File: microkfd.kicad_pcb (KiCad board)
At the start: 2 copper layers, 55 x 25.5 mm, 41 parts, among them J1 USB_B_Micro, J2 AudioJack3, J3 OLED, Q1 2N7002, Q2 2N7002, SW1 RST, SW2 DOWN, SW3 ENT, SW4 UP, U1 SP3003-02, U2 ATmega32U4-AU, Y1 16MHz

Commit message: rev A design done
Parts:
- added G***: LOGO, w3axl-logos:logo-4.2x4.2, B.Cu at (138.0, 94.5)
- added TP1: MOSI, TestPoint:TestPoint_Pad_1.0x1.0mm, B.Cu at (113.2, 110.0)
- added TP2: SCK, TestPoint:TestPoint_Pad_1.0x1.0mm, B.Cu at (115.2, 110.0)
- added TP3: MISO, TestPoint:TestPoint_Pad_1.0x1.0mm, B.Cu at (111.2, 110.0)
- added TP4: RST, TestPoint:TestPoint_Pad_1.0x1.0mm, B.Cu at (117.2, 110.0)
- added TP5: VCC, TestPoint:TestPoint_Pad_1.0x1.0mm, B.Cu at (109.2, 110.0)
- added TP6: GND, TestPoint:TestPoint_Pad_1.0x1.0mm, B.Cu at (119.2, 110.0)
- J1: footprint Connector_USB:USB_Mini-B_Wuerth_65100516121_Horizontal -> Connector_USB:USB_Micro-B_Wuerth_629105150521_CircularHoles
- moved D5 108.9 mm to (140.0, 109.8), turned to 90 degrees
- moved D4 103.8 mm to (134.0, 109.7), turned to 90 degrees
- moved R17 103.4 mm to (137.0, 109.8), turned to 270 degrees
- moved R16 98.9 mm to (131.0, 109.8), turned to 270 degrees
- moved R4 98.4 mm to (124.0, 110.8)
- moved R6 90.0 mm to (124.0, 108.5)
- moved C3 89.8 mm to (107.0, 104.5), turned to 270 degrees
- moved C6 75.0 mm to (99.0, 91.8)
- moved F1 4.74 mm to (94.5, 90.5), turned to 270 degrees
- moved C5 4.50 mm to (127.5, 109.8)
- moved U1 0.75 mm to (99.0, 109.8), turned to 180 degrees
- moved D2 0.56 mm to (137.8, 105.5)
- moved D3 0.56 mm to (93.2, 109.8)
- moved R14 0.56 mm to (133.2, 105.5)
- moved C1 0.35 mm to (119.2, 110.0)
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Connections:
- net Net-(R3-Pad1) renamed RST
- U2 pad 10: LED_PWR -> MOSI
- U2 pad 11: Net-(U2-Pad11) -> MISO
- U2 pad 12: Net-(U2-Pad12) -> LED_PWR
- U2 pad 9: Net-(U2-Pad9) -> SCK
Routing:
- net LED_ACT: track 0.00 -> 36.0 mm, vias 0 -> 2
- net I2C_SCL: track 0.00 -> 34.0 mm, vias 0 -> 2
- net I2C_SDA: track 0.00 -> 29.5 mm, vias 0 -> 2
- net RST: track 0.00 -> 27.9 mm, vias 0 -> 1
- net +5V: track 128.2 -> 148.9 mm, vias 6 -> 7
- net LED_PWR: track 0.00 -> 16.8 mm, vias 0 -> 2
- net Net-(J1-Pad2): track 11.4 -> 27.5 mm
- net LED_SNS: track 0.00 -> 15.1 mm, vias 0 -> 2
- net Net-(J1-Pad3): track 10.5 -> 22.9 mm
- net SCK: track 0.00 -> 11.1 mm, vias 0 -> 1
- net MOSI: track 0.00 -> 9.26 mm, vias 0 -> 1
- net MISO: track 0.00 -> 6.94 mm, vias 0 -> 1
- net Net-(C3-Pad1): track 0.00 -> 5.12 mm
- net Net-(D4-Pad2): track 0.00 -> 3.85 mm
- net Net-(D5-Pad2): track 0.00 -> 3.84 mm
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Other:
- board text added: "5V"
- board text added: "GND"
- board text added: "MISO"
- board text added: "MOSI"
- board text added: "MicroKFD"
- board text added: "RST"
- board text added: "SCK"
- board text added: "rev A 2021-12-06"

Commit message: cleanups and updates
- switched to Kicad 6.0
- removed Kicad 5.x files
- switched to 32u4RC due to availability
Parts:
- U2: value ATmega32U4-AU -> ATmega32U4RC-A
- moved G*** 0.25 mm to (137.8, 94.5), turned to 180 degrees
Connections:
- J1 pad 4: Net-(J1-Pad4) -> unconnected-(J1-Pad4)
- U1 pad 3: Net-(U1-Pad3) -> unconnected-(U1-Pad3)
- U2 pad 20: Net-(U2-Pad20) -> unconnected-(U2-Pad20)
- U2 pad 21: Net-(U2-Pad21) -> unconnected-(U2-Pad21)
- U2 pad 22: Net-(U2-Pad22) -> unconnected-(U2-Pad22)
- U2 pad 26: Net-(U2-Pad26) -> unconnected-(U2-Pad26)
- U2 pad 28: Net-(U2-Pad28) -> unconnected-(U2-Pad28)
- U2 pad 29: Net-(U2-Pad29) -> unconnected-(U2-Pad29)
- U2 pad 30: Net-(U2-Pad30) -> unconnected-(U2-Pad30)
- U2 pad 32: Net-(U2-Pad32) -> unconnected-(U2-Pad32)
- U2 pad 33: Net-(U2-Pad33) -> unconnected-(U2-Pad33)
- U2 pad 39: Net-(U2-Pad39) -> unconnected-(U2-Pad39)
- U2 pad 40: Net-(U2-Pad40) -> unconnected-(U2-Pad40)
- U2 pad 41: Net-(U2-Pad41) -> unconnected-(U2-Pad41)
- U2 pad 8: Net-(U2-Pad8) -> unconnected-(U2-Pad8)
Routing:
- net unconnected-(J1-Pad4): track 0.00 -> 1.92 mm
- net Net-(J1-Pad4): track 1.92 -> 0.00 mm
- net XT2: track 10.8 -> 10.1 mm
- net Net-(U1-Pad3): track 0.65 -> 0.00 mm
- net unconnected-(U1-Pad3): track 0.00 -> 0.60 mm
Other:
- net class Default removed
- board text added: "rev B 2022-01-08"
- board text removed: "rev A 2021-12-06"

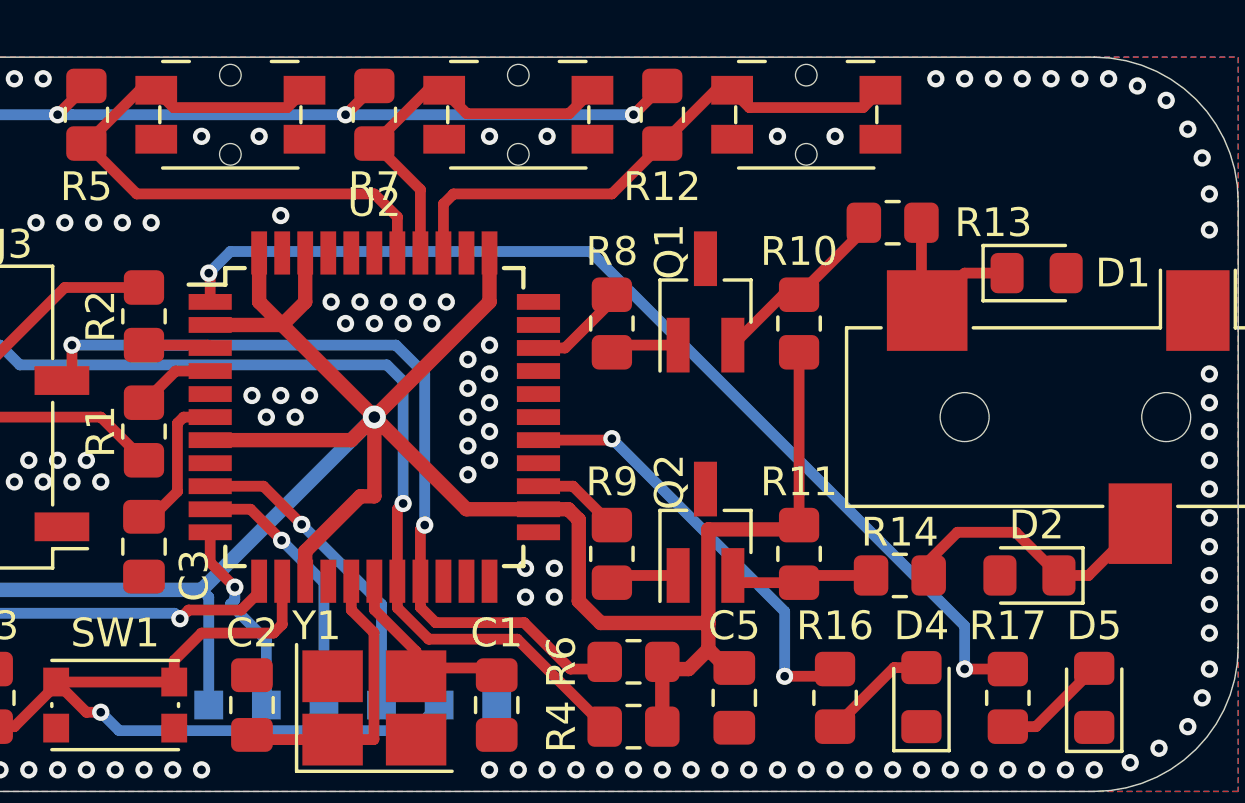
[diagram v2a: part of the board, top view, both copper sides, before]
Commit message: finalized rev B
switched MOSFETs due to parts availability, regenerated gerbers
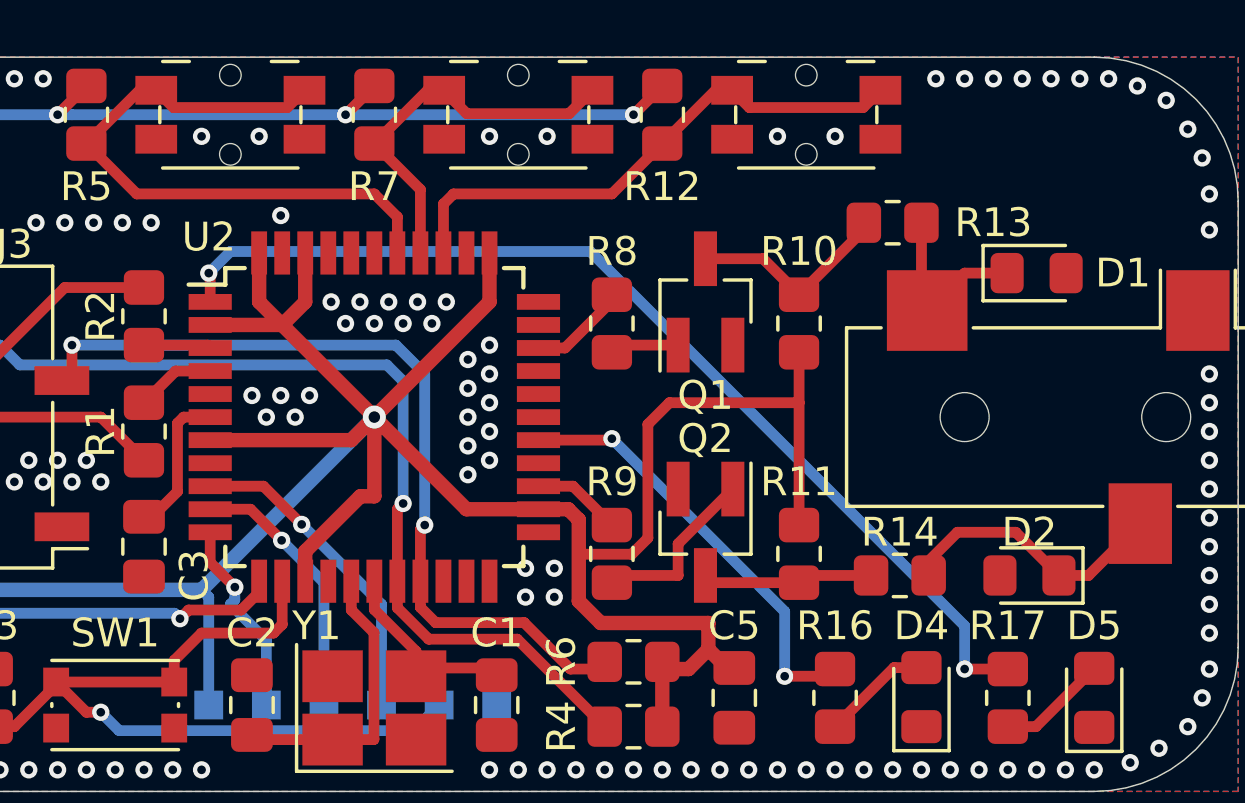
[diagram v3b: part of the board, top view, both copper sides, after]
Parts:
- Q1, Q2: value 2N7002 -> T2N7002
- moved G*** 0.25 mm to (138.0, 94.5)
- turned Q2 to -90 degrees
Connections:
- Q1 pad 2: Net-(Q1-Pad2) -> GND
- Q1 pad 3: GND -> Net-(R10-Pad1)
- Q2 pad 2: Net-(Q2-Pad2) -> GND
- Q2 pad 3: GND -> Net-(R11-Pad1)
- R10 pad 1: Net-(Q1-Pad2) -> Net-(R10-Pad1)
- R11 pad 1: Net-(Q2-Pad2) -> Net-(R11-Pad1)
- R13 pad 1: Net-(Q1-Pad2) -> Net-(R10-Pad1)
- R14 pad 1: Net-(Q2-Pad2) -> Net-(R11-Pad1)
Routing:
- net Net-(R10-Pad1): track 0.00 -> 7.20 mm
- net Net-(Q1-Pad2): track 6.46 -> 0.00 mm
- net Net-(R11-Pad1): track 0.00 -> 5.96 mm
- net +5V: track 148.5 -> 154.1 mm
- net Net-(Q2-Pad2): track 5.01 -> 0.00 mm
- net Net-(R9-Pad1): track 2.40 -> 6.19 mm

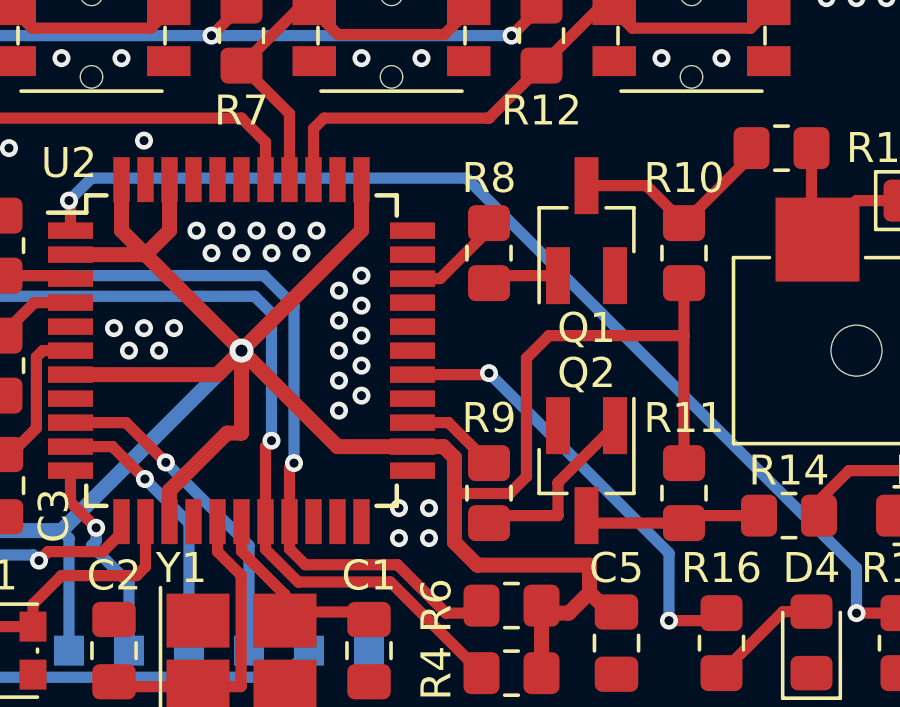
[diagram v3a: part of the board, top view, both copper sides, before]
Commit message: revC updates
fixed missing data input line (now runs to PC2 interrupt pin)
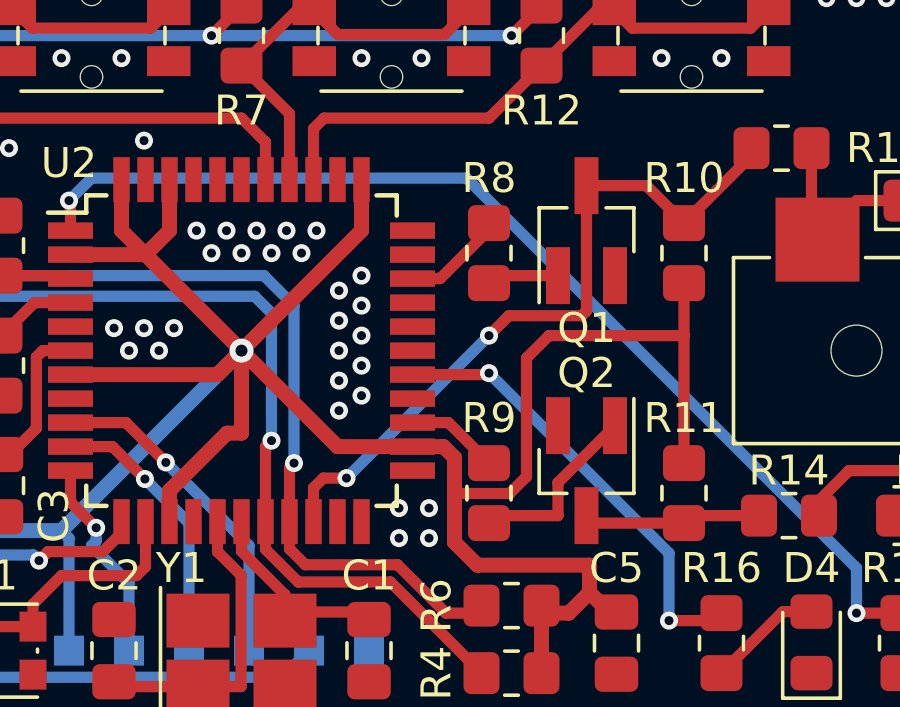
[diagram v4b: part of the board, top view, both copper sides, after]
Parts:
- moved G*** 0.35 mm to (137.8, 94.2)
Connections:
- net DATA renamed DATA_OUT
- Q1 pad 3: Net-(R10-Pad1) -> DATA_IN
- R10 pad 1: Net-(R10-Pad1) -> DATA_IN
- R13 pad 1: Net-(R10-Pad1) -> DATA_IN
- U2 pad 20: unconnected-(U2-Pad20) -> DATA_IN
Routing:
- net DATA_IN: track 0.00 -> 24.0 mm, vias 0 -> 2
- net Net-(R10-Pad1): track 7.20 -> 0.00 mm
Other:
- board text added: "rev C 2022-01-19"
- board text removed: "rev B 2022-01-08"

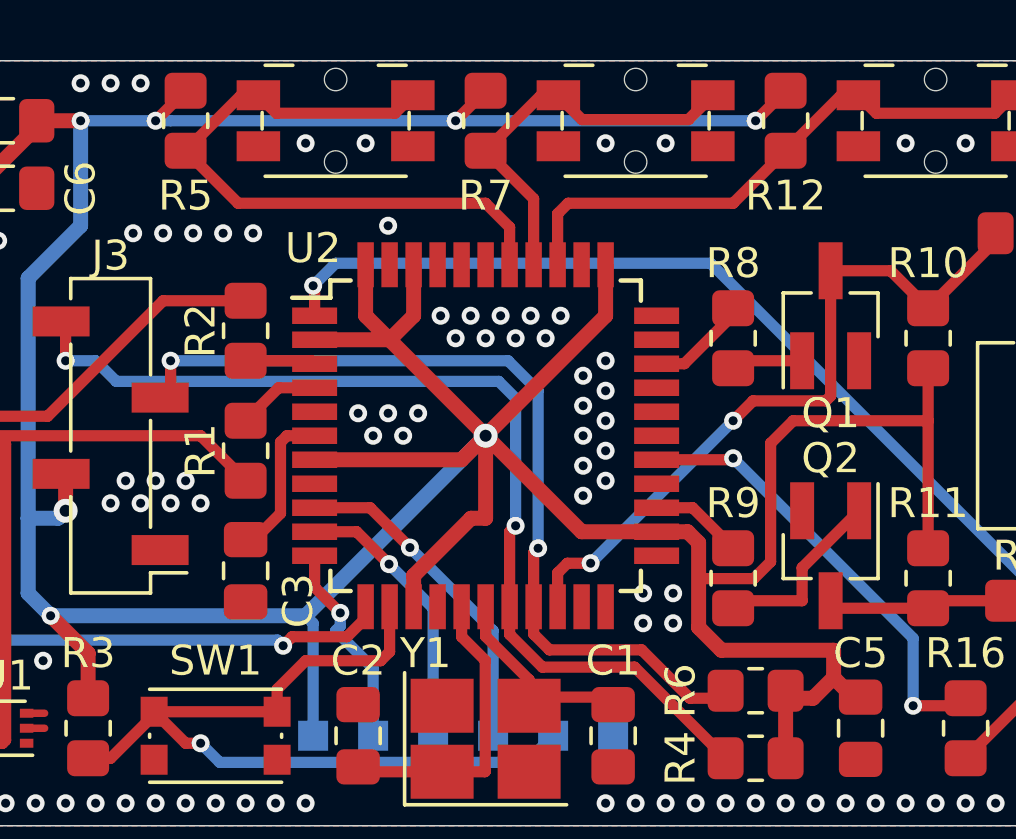
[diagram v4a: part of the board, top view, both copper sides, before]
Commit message: rev D: fixed pin mappings
changed pin mappings to be closer to original KFDShield, added correct sense and data lines
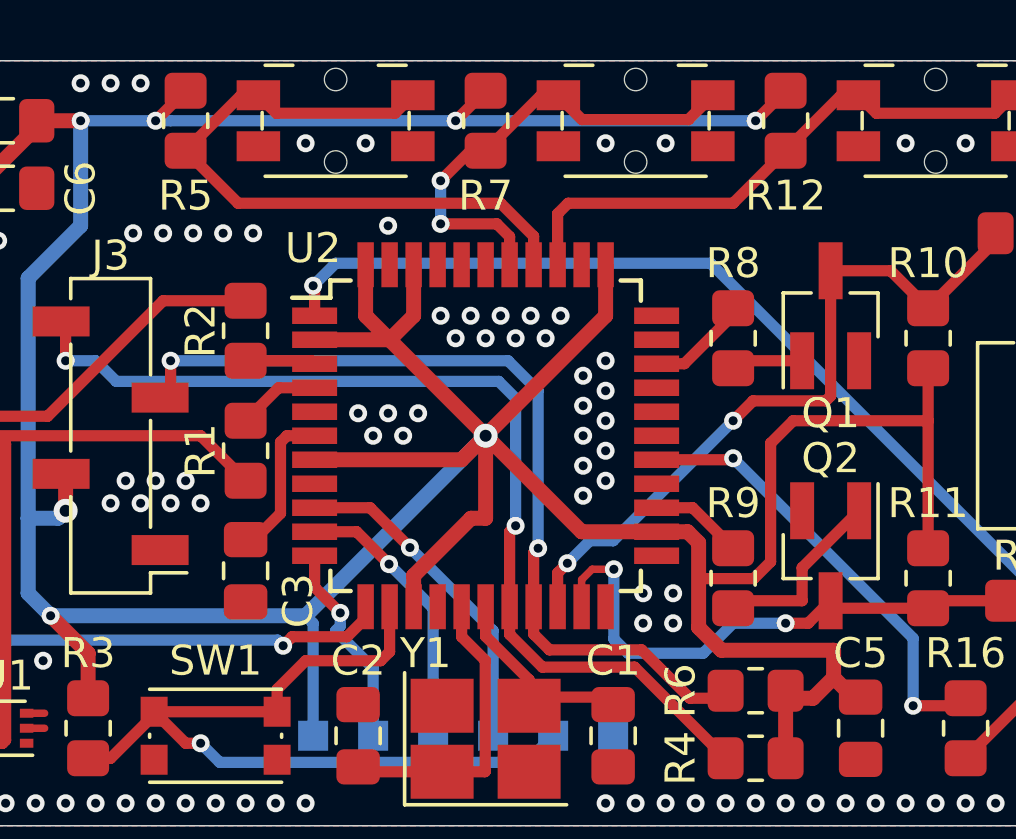
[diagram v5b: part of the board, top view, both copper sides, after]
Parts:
- removed G***: LOGO, w3axl-logos:logo-4.2x4.2
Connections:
- net SENSE renamed SENSE_OUT
- Q2 pad 3: Net-(Q2-Pad3) -> SENSE_IN
- R11 pad 1: Net-(Q2-Pad3) -> SENSE_IN
- R14 pad 1: Net-(Q2-Pad3) -> SENSE_IN
- U2 pad 21: unconnected-(U2-Pad21) -> SENSE_IN
- U2 pad 37: SW_ENT -> SW_DN
- U2 pad 38: SW_DN -> SW_ENT
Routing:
- net SENSE_IN: track 0.00 -> 18.5 mm, vias 0 -> 2
- net Net-(Q2-Pad3): track 5.96 -> 0.00 mm
- net SW_ENT: track 13.5 -> 15.8 mm, vias 0 -> 2
- net SW_DN: track 21.9 -> 22.6 mm

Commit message: added logo to PCB
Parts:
- added G***: LOGO, w3axl-logos:logo-4.2x4.2, B.Cu at (137.8, 94.2)

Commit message: updated gerbers for logo change
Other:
- board text added: "rev D 2022-04-09"
- board text removed: "rev C 2022-01-19"
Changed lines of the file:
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@@
     (effects (font (size 2 2) (thickness 0.25)) (justify left mirror))
   )
-  (gr_text "rev C 2022-01-19" (at 134.75 95.75) (layer "B.SilkS")
+  (gr_text "rev D 2022-04-09" (at 134.75 95.75) (layer "B.SilkS")
     (effects (font (size 1 1) (thickness 0.15)) (justify left mirror))
   )
